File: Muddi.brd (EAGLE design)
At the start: 85.1 x 78.4 mm, 8 parts, among them J1 DCJ0202

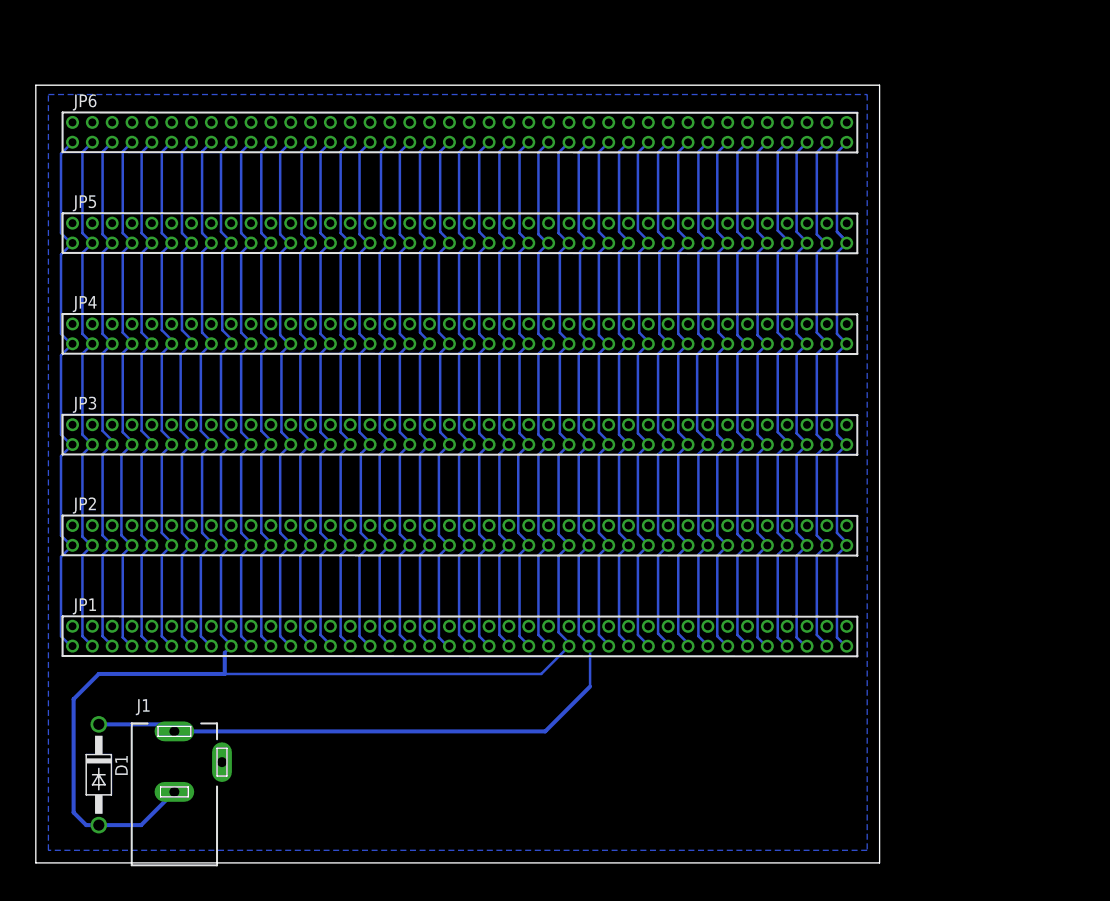
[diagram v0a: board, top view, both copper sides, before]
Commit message: Move away Serial CF
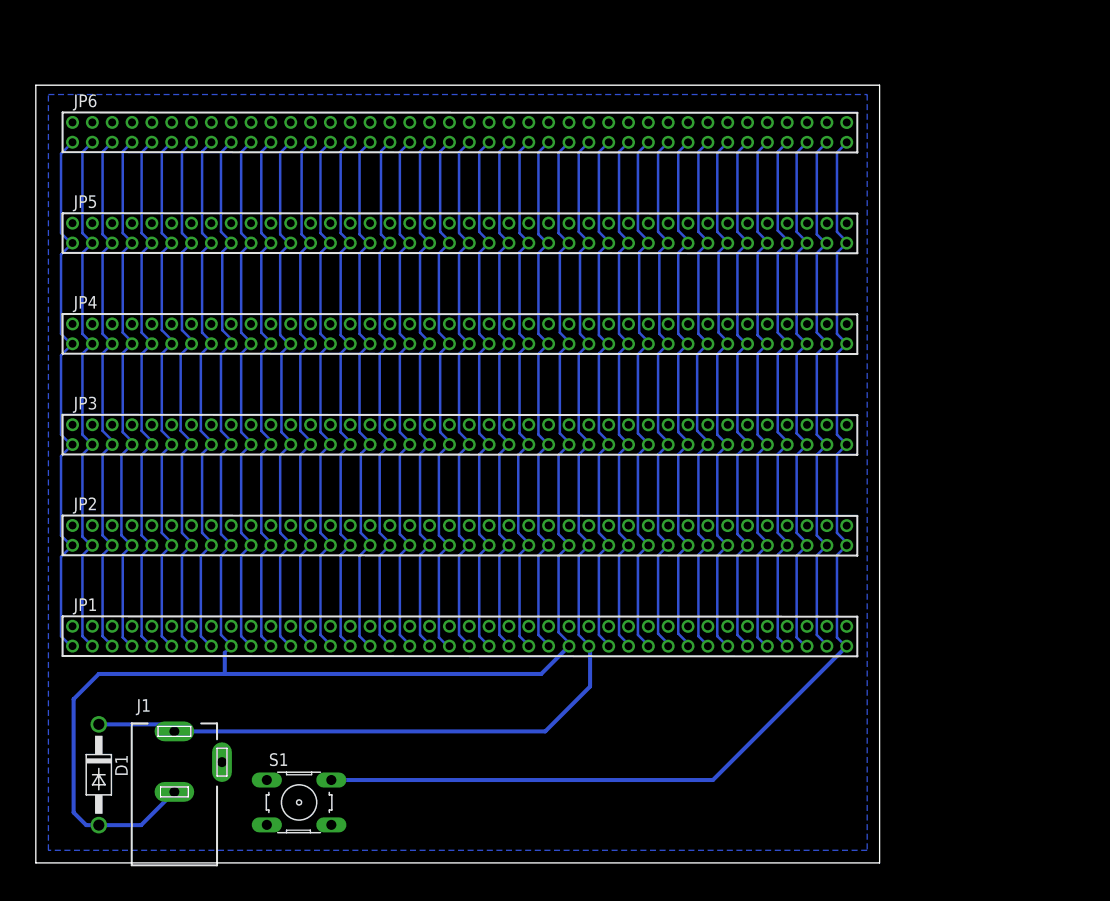
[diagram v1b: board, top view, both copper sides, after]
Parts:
- added S1: RESET, switch-omron:B3F-10XX
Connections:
- net GND: now also S1.3
- net N$40: now also S1.1, S1.2
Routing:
- net N$40: track 56.5 -> 112.5 mm
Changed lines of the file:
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@@
 <element name="JP5" library="jean" package="57102-F08-25" value="" x="11.43" y="63.5"/>
 <element name="JP6" library="jean" package="57102-F08-25" value="" x="11.43" y="73.66"/>
+<element name="S1" library="switch-omron" package="B3F-10XX" value="RESET" x="25.273" y="6.096">
+<attribute name="OC_FARNELL" value="176432" x="25.273" y="6.096" size="1.778" layer="27" display="off"/>
+<attribute name="OC_NEWARK" value="36M3542" x="25.273" y="6.096" size="1.778" layer="27" display="off"/>
+<attribute name="MPN" value="B3F-1000" x="25.273" y="6.096" size="1.778" layer="27" display="off"/>
+<attribute name="MF" value="OMRON ELECTRONIC COMPONENTS" x="25.273" y="6.096" size="1.778" layer="27" display="off"/>
+</element>
 </elements>
 <signals>
@@
 <wire x1="79.502" y1="61.5049125" x2="80.48644375" y2="62.48935625" width="0.254" layer="16"/>
 <wire x1="80.48644375" y1="62.48935625" x2="80.48644375" y2="62.64255625" width="0.254" layer="16"/>
-<wire x1="79.502" y1="63.627" x2="80.48644375" y2="62.64255625" width="0.254" layer="16"/>
-<wire x1="80.48644375" y1="62.48935625" x2="80.48644375" y2="62.64255625" width="0.254" layer="16"/>
 <wire x1="80.48644375" y1="62.64255625" x2="79.502" y2="63.627" width="0.254" layer="16"/>
 <wire x1="80.48644375" y1="72.64935625" x2="80.48644375" y2="72.61244375" width="0.254" layer="16"/>
 <wire x1="80.48644375" y1="72.61244375" x2="79.502" y2="71.628" width="0.254" layer="16"/>
 <wire x1="79.502" y1="71.628" x2="79.502" y2="63.627" width="0.254" layer="16"/>
+<contactref element="S1" pad="1"/>
+<contactref element="S1" pad="2"/>
+<wire x1="28.5242" y1="8.3566" x2="66.9936875" y2="8.3566" width="0.4064" layer="16"/>
+<wire x1="66.9936875" y1="8.3566" x2="80.48644375" y2="21.84935625" width="0.4064" layer="16"/>
+<wire x1="22.0218" y1="8.3566" x2="28.5242" y2="8.3566" width="0" layer="19" extent="1-1"/>
 </signal>
 <signal name="N$41">
@@
 <wire x1="12.7" y1="13.26" x2="50.09" y2="13.26" width="0.4064" layer="16"/>
 <wire x1="50.09" y1="13.26" x2="54.61" y2="17.78" width="0.4064" layer="16"/>
-<wire x1="54.61" y1="17.78" x2="54.61" y2="21.7258" width="0.254" layer="16"/>
+<wire x1="54.61" y1="17.78" x2="54.61" y2="21.7258" width="0.4064" layer="16"/>
 <wire x1="54.61" y1="21.7258" x2="54.48644375" y2="21.84935625" width="0.254" layer="16"/>
 <wire x1="54.48644375" y1="21.84935625" x2="54.48644375" y2="21.96755625" width="0.254" layer="16"/>
@@
 <wire x1="51.435" y1="63.5" x2="51.435" y2="71.5979125" width="0.254" layer="16"/>
 <wire x1="51.435" y1="71.5979125" x2="52.48644375" y2="72.64935625" width="0.254" layer="16"/>
-<wire x1="17.78" y1="19.05" x2="49.6870875" y2="19.05" width="0.254" layer="16"/>
-<wire x1="49.6870875" y1="19.05" x2="52.48644375" y2="21.84935625" width="0.254" layer="16"/>
+<wire x1="17.78" y1="19.05" x2="49.6870875" y2="19.05" width="0.4064" layer="16"/>
+<wire x1="49.6870875" y1="19.05" x2="52.48644375" y2="21.84935625" width="0.4064" layer="16"/>
 <polygon width="0.254" layer="16">
 <vertex x="0" y="77.47"/>
@@
 <vertex x="0" y="1.27"/>
 </polygon>
+<contactref element="S1" pad="3"/>
 </signal>
 </signals>

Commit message: Finish Modularization
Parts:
- added LED1: (no value), led:LED5MM
- added R1: (no value), resistor:0207/2V
- added U$1: (no value), bfl:OSHW1
- moved JP6 6.35 mm to (11.4, 80.0)
- moved JP5 5.08 mm to (11.4, 68.6)
- moved JP4 3.81 mm to (11.4, 57.1)
- moved JP3 2.54 mm to (11.4, 45.7)
- moved JP2 1.27 mm to (11.4, 34.3)
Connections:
- new net N$25: LED1.A, R1.1
- net GND: now also LED1.K
- net VCC: now also R1.2
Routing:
- net VCC: track 110.7 -> 181.8 mm
- net N$40: track 112.5 -> 125.4 mm
- net GND: track 188.7 -> 201.4 mm
- net N$22: track 54.8 -> 61.1 mm
- net N$7: track 54.9 -> 61.3 mm
- net N$6: track 54.9 -> 61.3 mm
- net N$48: track 55.0 -> 61.3 mm
- net N$47: track 54.9 -> 61.2 mm
- net N$45: track 54.9 -> 61.3 mm
- net N$39: track 55.3 -> 61.6 mm
- net N$38: track 55.1 -> 61.4 mm
- net N$23: track 54.8 -> 61.1 mm
- net N$16: track 55.0 -> 61.3 mm
- net N$9: track 54.9 -> 61.3 mm
- net N$8: track 54.9 -> 61.3 mm
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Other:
- board size 85.1 x 78.4 mm -> 85.1 x 84.8 mm
- board text added: "CPD-80 MUDDI V1"

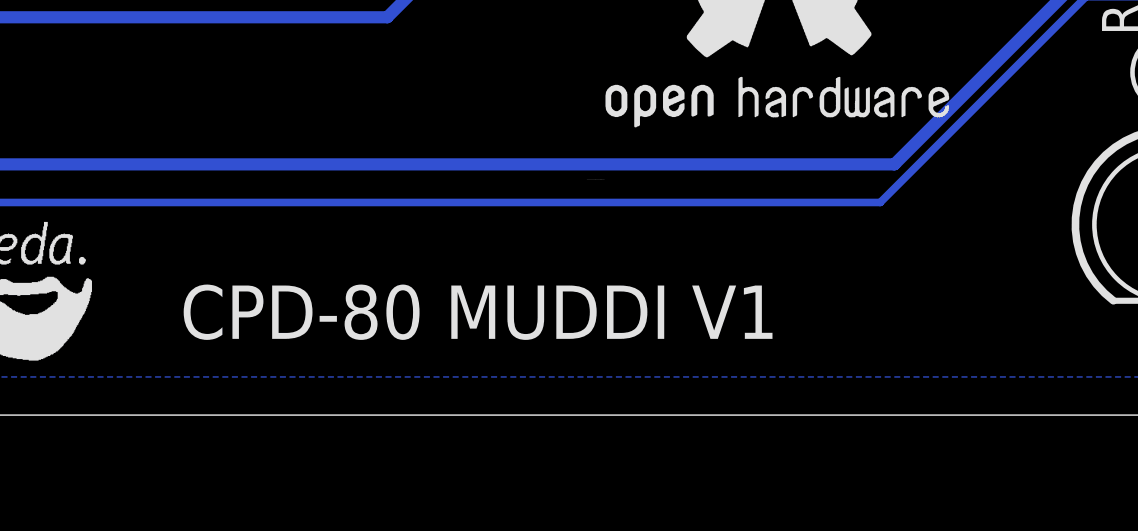
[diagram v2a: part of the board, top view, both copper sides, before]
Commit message: Update names and font
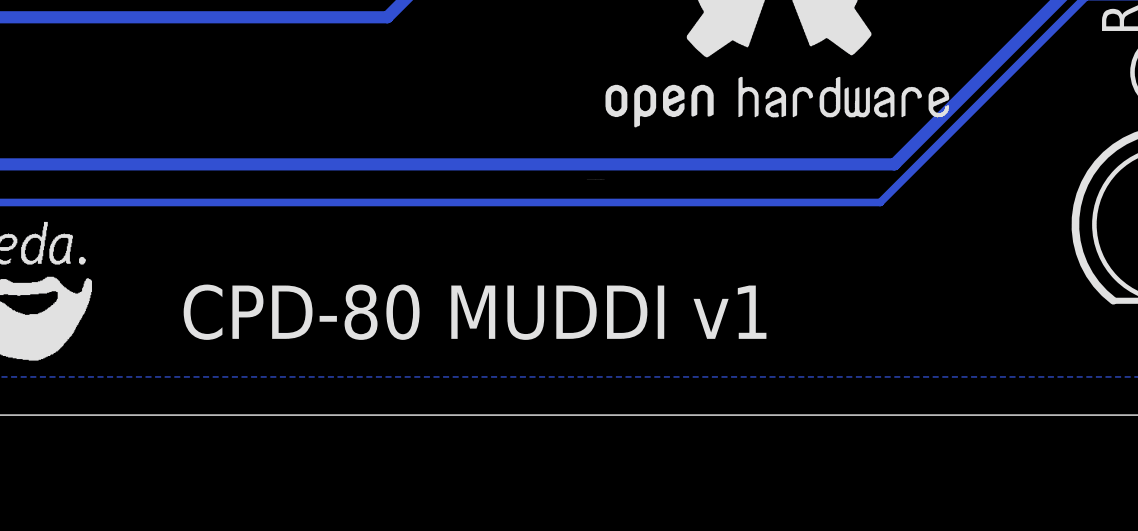
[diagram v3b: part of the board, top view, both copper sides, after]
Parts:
- LED1: value (none) -> BW
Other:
- board text added: "CPD-80 MUDDI v1"
- board text removed: "CPD-80 MUDDI V1"
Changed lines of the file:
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@@
 <wire x1="83.8" y1="84.76" x2="-1.27" y2="84.76" width="0" layer="20"/>
 <wire x1="-1.27" y1="84.76" x2="-1.27" y2="0" width="0" layer="20"/>
-<text x="43.18" y="2.54" size="1.778" layer="21">CPD-80 MUDDI V1</text>
+<text x="43.18" y="2.54" size="1.778" layer="21" font="fixed">CPD-80 MUDDI v1</text>
 <rectangle x1="38.1381" y1="1.8161" x2="38.4683" y2="1.8415" layer="21"/>
 <rectangle x1="37.9349" y1="1.8415" x2="38.5445" y2="1.8669" layer="21"/>
@@
 <attribute name="MF" value="OMRON ELECTRONIC COMPONENTS" x="25.273" y="6.096" size="1.778" layer="27" display="off"/>
 </element>
-<element name="LED1" library="led" package="LED5MM" value="" x="76.2" y="6.35" rot="R270"/>
+<element name="LED1" library="led" package="LED5MM" value="BW" x="76.2" y="6.35" rot="R270"/>
 <element name="R1" library="resistor" package="0207/2V" value="" x="76.2" y="12.7" rot="R90"/>
 <element name="U$1" library="bfl" package="OSHW1" value="" x="56.7436" y="7.874"/>

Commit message: Add Resistor Value
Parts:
- R1: value (none) -> 560
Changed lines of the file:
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@@
 </element>
 <element name="LED1" library="led" package="LED5MM" value="BW" x="76.2" y="6.35" rot="R270"/>
-<element name="R1" library="resistor" package="0207/2V" value="" x="76.2" y="12.7" rot="R90"/>
+<element name="R1" library="resistor" package="0207/2V" value="560" x="76.2" y="12.7" rot="R90"/>
 <element name="U$1" library="bfl" package="OSHW1" value="" x="56.7436" y="7.874"/>
 </elements>

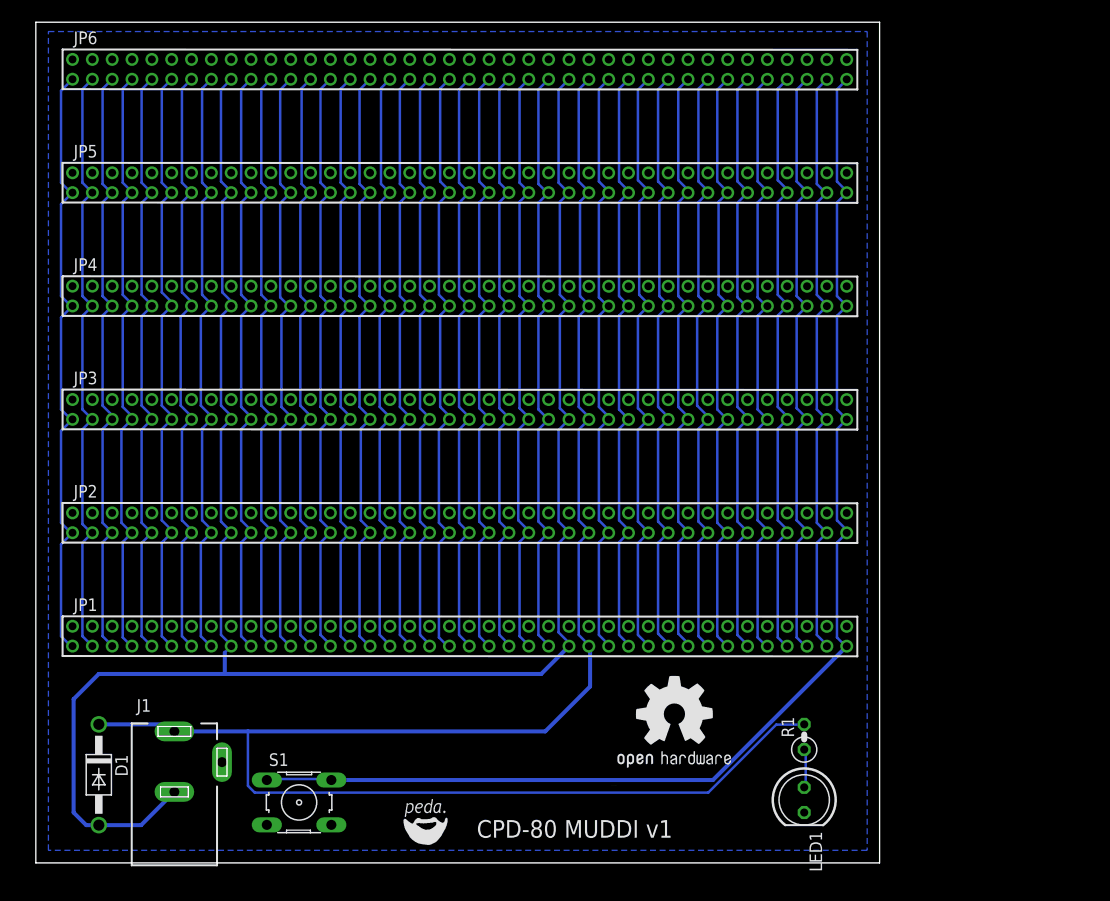
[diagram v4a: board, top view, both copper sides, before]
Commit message: Fix MUDDI. Change values to mm.
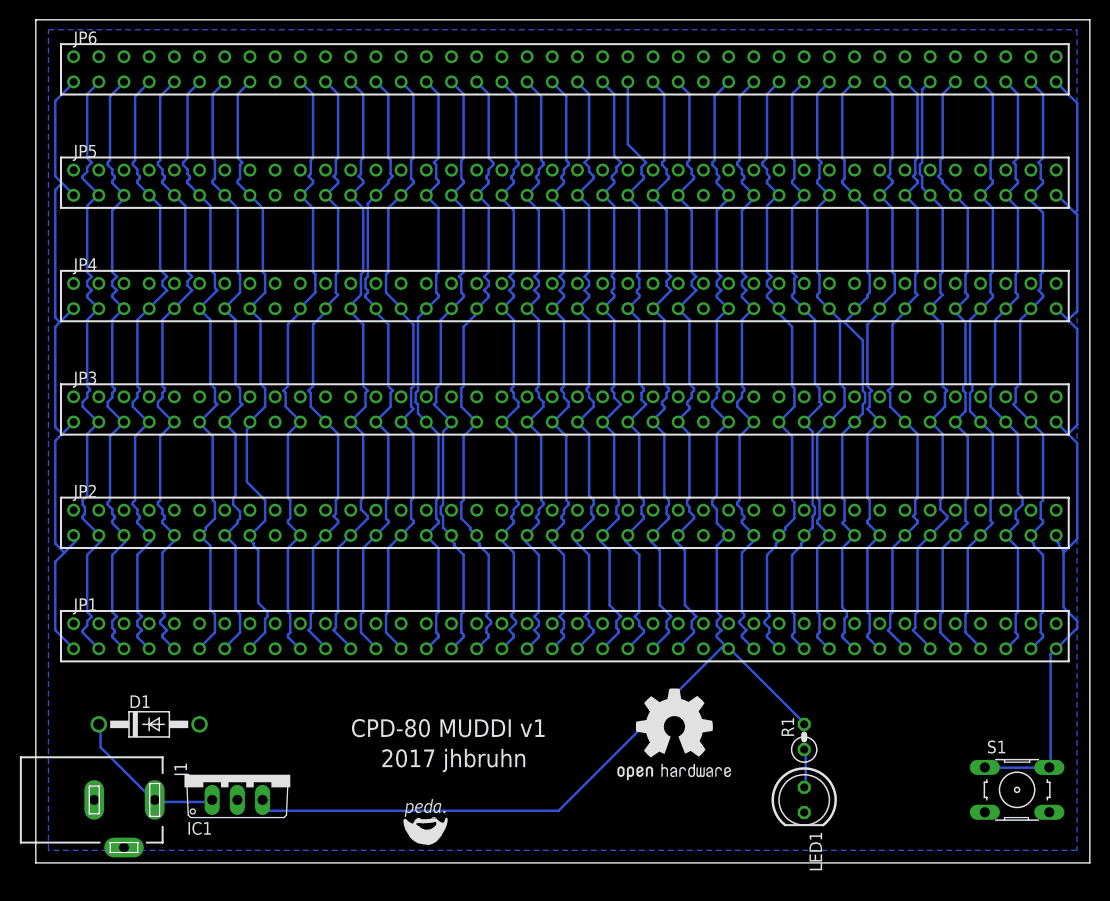
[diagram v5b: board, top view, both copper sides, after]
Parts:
- added IC1: 7805TV, linear:TO220V
- moved S1 72.4 mm to (97.7, 7.37)
- moved D1 7.18 mm to (10.2, 14.0), turned to 0 degrees
- moved J1 6.35 mm to (7.62, 6.35), turned to 270 degrees
- moved U$1 1.27 mm to (56.7, 6.60)
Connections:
- new net N$26: D1.C, IC1.1, J1.1
- net GND: now also IC1.2
- net VCC: now also IC1.3; no longer D1.C, J1.1
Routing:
- net GND: track 201.4 -> 0.13 mm
- net VCC: track 181.8 -> 131.6 mm
- net N$40: track 125.4 -> 88.7 mm
- net N$26: track 0.00 -> 16.2 mm
- net N$1: track 62.4 -> 68.8 mm
- net N$4: track 61.2 -> 66.0 mm
- net N$23: track 61.1 -> 65.9 mm
- net N$18: track 61.1 -> 65.8 mm
- net N$2: track 61.4 -> 65.9 mm
- net N$20: track 61.5 -> 65.9 mm
- net N$21: track 61.3 -> 65.7 mm
- net N$5: track 61.5 -> 65.9 mm
- net N$24: track 61.5 -> 65.9 mm
- net N$3: track 61.2 -> 65.6 mm
- net N$22: track 61.1 -> 65.5 mm
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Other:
- board size 85.1 x 84.8 mm -> 106.3 x 85 mm
- board text added: "2017 jhbruhn"

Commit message: Add Ground Rail to JEANNECTOR
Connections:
- net GND: now also JP1.10, JP1.12, JP1.14, JP1.16, JP1.18, JP1.2, JP1.20, JP1.22, JP1.24, JP1.26, JP1.28, JP1.30, JP1.32, JP1.34, JP1.36, JP1.38, JP1.4, JP1.40, JP1.42, JP1.44, JP1.46, JP1.48, JP1.50, JP1.52, JP1.54, JP1.56, JP1.58, JP1.6, JP1.60, JP1.62, JP1.64, JP1.66, JP1.68, JP1.70, JP1.72, JP1.74, JP1.76, JP1.78, JP1.8, JP1.80, JP2.10, JP2.12, JP2.14, JP2.16, JP2.18, JP2.2, JP2.20, JP2.22, JP2.24, JP2.26, JP2.28, JP2.30, JP2.32, JP2.34, JP2.36, JP2.38, JP2.4, JP2.40, JP2.42, JP2.44, JP2.46, JP2.48, JP2.50, JP2.52, JP2.54, JP2.56, JP2.58, JP2.6, JP2.60, JP2.62, JP2.64, JP2.66, JP2.68, JP2.70, JP2.72, JP2.74, JP2.76, JP2.78, JP2.8, JP2.80, JP3.10, JP3.12, JP3.14, JP3.16, JP3.18, JP3.2, JP3.20, JP3.22, JP3.24, JP3.26, JP3.28, JP3.30, JP3.32, JP3.34, JP3.36, JP3.38, JP3.4, JP3.40, JP3.42, JP3.44, JP3.46, JP3.48, JP3.50, JP3.52, JP3.54, JP3.56, JP3.58, JP3.6, JP3.60, JP3.62, JP3.64, JP3.66, JP3.68, JP3.70, JP3.72, JP3.74, JP3.76, JP3.78, JP3.8, JP3.80, JP4.10, JP4.12, JP4.14, JP4.16, JP4.18, JP4.2, JP4.20, JP4.22, JP4.24, JP4.26, JP4.28, JP4.30, JP4.32, JP4.34, JP4.36, JP4.38, JP4.4, JP4.40, JP4.42, JP4.44, JP4.46, JP4.48, JP4.50, JP4.52, JP4.54, JP4.56, JP4.58, JP4.6, JP4.60, JP4.62, JP4.64, JP4.66, JP4.68, JP4.70, JP4.72, JP4.74, JP4.76, JP4.78, JP4.8, JP4.80, JP5.10, JP5.12, JP5.14, JP5.16, JP5.18, JP5.2, JP5.20, JP5.22, JP5.24, JP5.26, JP5.28, JP5.30, JP5.32, JP5.34, JP5.36, JP5.38, JP5.4, JP5.40, JP5.42, JP5.44, JP5.46, JP5.48, JP5.50, JP5.52, JP5.54, JP5.56, JP5.58, JP5.6, JP5.60, JP5.62, JP5.64, JP5.66, JP5.68, JP5.70, JP5.72, JP5.74, JP5.76, JP5.78, JP5.8, JP5.80, JP6.10, JP6.12, JP6.14, JP6.16, JP6.18, JP6.2, JP6.20, JP6.22, JP6.24, JP6.26, JP6.28, JP6.30, JP6.32, JP6.34, JP6.36, JP6.38, JP6.4, JP6.40, JP6.42, JP6.44, JP6.46, JP6.48, JP6.50, JP6.52, JP6.54, JP6.56, JP6.58, JP6.6, JP6.60, JP6.62, JP6.64, JP6.66, JP6.68, JP6.70, JP6.72, JP6.74, JP6.76, JP6.78, JP6.8, JP6.80
